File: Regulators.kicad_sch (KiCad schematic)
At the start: 34 parts, among them J3 Conn_01x02_Socket, U10 TPS5430DDAR, U2 TPS5430DDAR, U9 TPS5430DDAR

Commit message: Initial tidy of untracked files
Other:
- note added: "Todo - redo regulators once you know the current draw of all device, ideally within the 60-70% range of current limit for peak efficiency"
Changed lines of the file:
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@@
+		)
+	)
+	(text "Todo - redo regulators once you know the current draw of all device, \nideally within the 60-70% range of current limit for peak efficiency"
+		(exclude_from_sim no)
+		(at 161.036 19.304 0)
+		(effects
+			(font
+				(size 1.27 1.27)
+			)
 		)
 	)

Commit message: Changed board spec from Nucleo F446RE to F446ZE Altered readme to suit it and moved the Todos over.
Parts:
- C16, C17, C18, C2, C20, C21: footprint (none) -> Capacitor_SMD:C_1206_3216Metric_Pad1.33x1.80mm_HandSolder
- D1, D2, D3, D6, D7, D8: footprint (none) -> Diode_SMD:D_1206_3216Metric_Pad1.42x1.75mm_HandSolder
- R10, R11, R2, R3, R4, R5, R6, R8, R9: footprint (none) -> Resistor_SMD:R_1206_3216Metric_Pad1.30x1.75mm_HandSolder
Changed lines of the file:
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@@
 			)
 		)
-		(property "Footprint" ""
+		(property "Footprint" "Resistor_SMD:R_1206_3216Metric_Pad1.30x1.75mm_HandSolder"
 			(at 131.826 117.094 90)
 			(effects
@@
 			)
 		)
-		(property "Footprint" ""
+		(property "Footprint" "Resistor_SMD:R_1206_3216Metric_Pad1.30x1.75mm_HandSolder"
 			(at 199.136 77.724 90)
 			(effects
@@
 			)
 		)
-		(property "Footprint" ""
+		(property "Footprint" "Capacitor_SMD:C_1206_3216Metric_Pad1.33x1.80mm_HandSolder"
 			(at 85.09 108.2548 0)
 			(effects
@@
 			)
 		)
-		(property "Footprint" ""
+		(property "Footprint" "Capacitor_SMD:C_1206_3216Metric_Pad1.33x1.80mm_HandSolder"
 			(at 101.2952 53.34 0)
 			(effects
@@
 			)
 		)
-		(property "Footprint" ""
+		(property "Footprint" "Capacitor_SMD:C_1206_3216Metric_Pad1.33x1.80mm_HandSolder"
 			(at 152.4 42.2148 0)
 			(effects
@@
 			)
 		)
-		(property "Footprint" ""
+		(property "Footprint" "Resistor_SMD:R_1206_3216Metric_Pad1.30x1.75mm_HandSolder"
 			(at 265.176 117.094 90)
 			(effects
@@
 			)
 		)
-		(property "Footprint" ""
+		(property "Footprint" "Capacitor_SMD:C_1206_3216Metric_Pad1.33x1.80mm_HandSolder"
 			(at 33.9852 119.38 0)
 			(effects
@@
 			)
 		)
-		(property "Footprint" ""
+		(property "Footprint" "Resistor_SMD:R_1206_3216Metric_Pad1.30x1.75mm_HandSolder"
 			(at 265.176 143.764 90)
 			(effects
@@
 			)
 		)
-		(property "Footprint" ""
+		(property "Footprint" "Resistor_SMD:R_1206_3216Metric_Pad1.30x1.75mm_HandSolder"
 			(at 253.746 42.164 90)
 			(effects
@@
 			)
 		)
-		(property "Footprint" ""
+		(property "Footprint" "Diode_SMD:D_1206_3216Metric_Pad1.42x1.75mm_HandSolder"
 			(at 252.73 52.07 0)
 			(effects
@@
 			)
 		)
-		(property "Footprint" ""
+		(property "Footprint" "Diode_SMD:D_1206_3216Metric_Pad1.42x1.75mm_HandSolder"
 			(at 237.49 52.07 0)
 			(effects
@@
 			)
 		)
-		(property "Footprint" ""
+		(property "Footprint" "Diode_SMD:D_1206_3216Metric_Pad1.42x1.75mm_HandSolder"
 			(at 267.97 52.07 0)
 			(effects
@@
 			)
 		)
-		(property "Footprint" ""
+		(property "Footprint" "Capacitor_SMD:C_1206_3216Metric_Pad1.33x1.80mm_HandSolder"
 			(at 218.44 108.2548 0)
 			(effects
@@
 			)
 		)
-		(property "Footprint" ""
+		(property "Footprint" "Diode_SMD:D_1206_3216Metric_Pad1.42x1.75mm_HandSolder"
 			(at 165.1 52.07 0)
 			(effects
@@
 			)
 		)
-		(property "Footprint" ""
+		(property "Footprint" "Capacitor_SMD:C_1206_3216Metric_Pad1.33x1.80mm_HandSolder"
 			(at 167.3352 119.38 0)
 			(effects
@@
 			)
 		)
-		(property "Footprint" ""
+		(property "Footprint" "Resistor_SMD:R_1206_3216Metric_Pad1.30x1.75mm_HandSolder"
 			(at 131.826 143.764 90)
 			(effects
@@
 			)
 		)
-		(property "Footprint" ""
+		(property "Footprint" "Resistor_SMD:R_1206_3216Metric_Pad1.30x1.75mm_HandSolder"
 			(at 199.136 51.054 90)
 			(effects
@@
 			)
 		)
-		(property "Footprint" ""
+		(property "Footprint" "Diode_SMD:D_1206_3216Metric_Pad1.42x1.75mm_HandSolder"
 			(at 97.79 118.11 0)
 			(effects
@@
 			)
 		)
-		(property "Footprint" ""
+		(property "Footprint" "Resistor_SMD:R_1206_3216Metric_Pad1.30x1.75mm_HandSolder"
 			(at 238.506 42.164 90)
 			(effects
@@
 			)
 		)
-		(property "Footprint" ""
+		(property "Footprint" "Diode_SMD:D_1206_3216Metric_Pad1.42x1.75mm_HandSolder"
 			(at 231.14 118.11 0)
 			(effects
@@
 			)
 		)
-		(property "Footprint" ""
+		(property "Footprint" "Resistor_SMD:R_1206_3216Metric_Pad1.30x1.75mm_HandSolder"
 			(at 268.986 42.164 90)
 			(effects

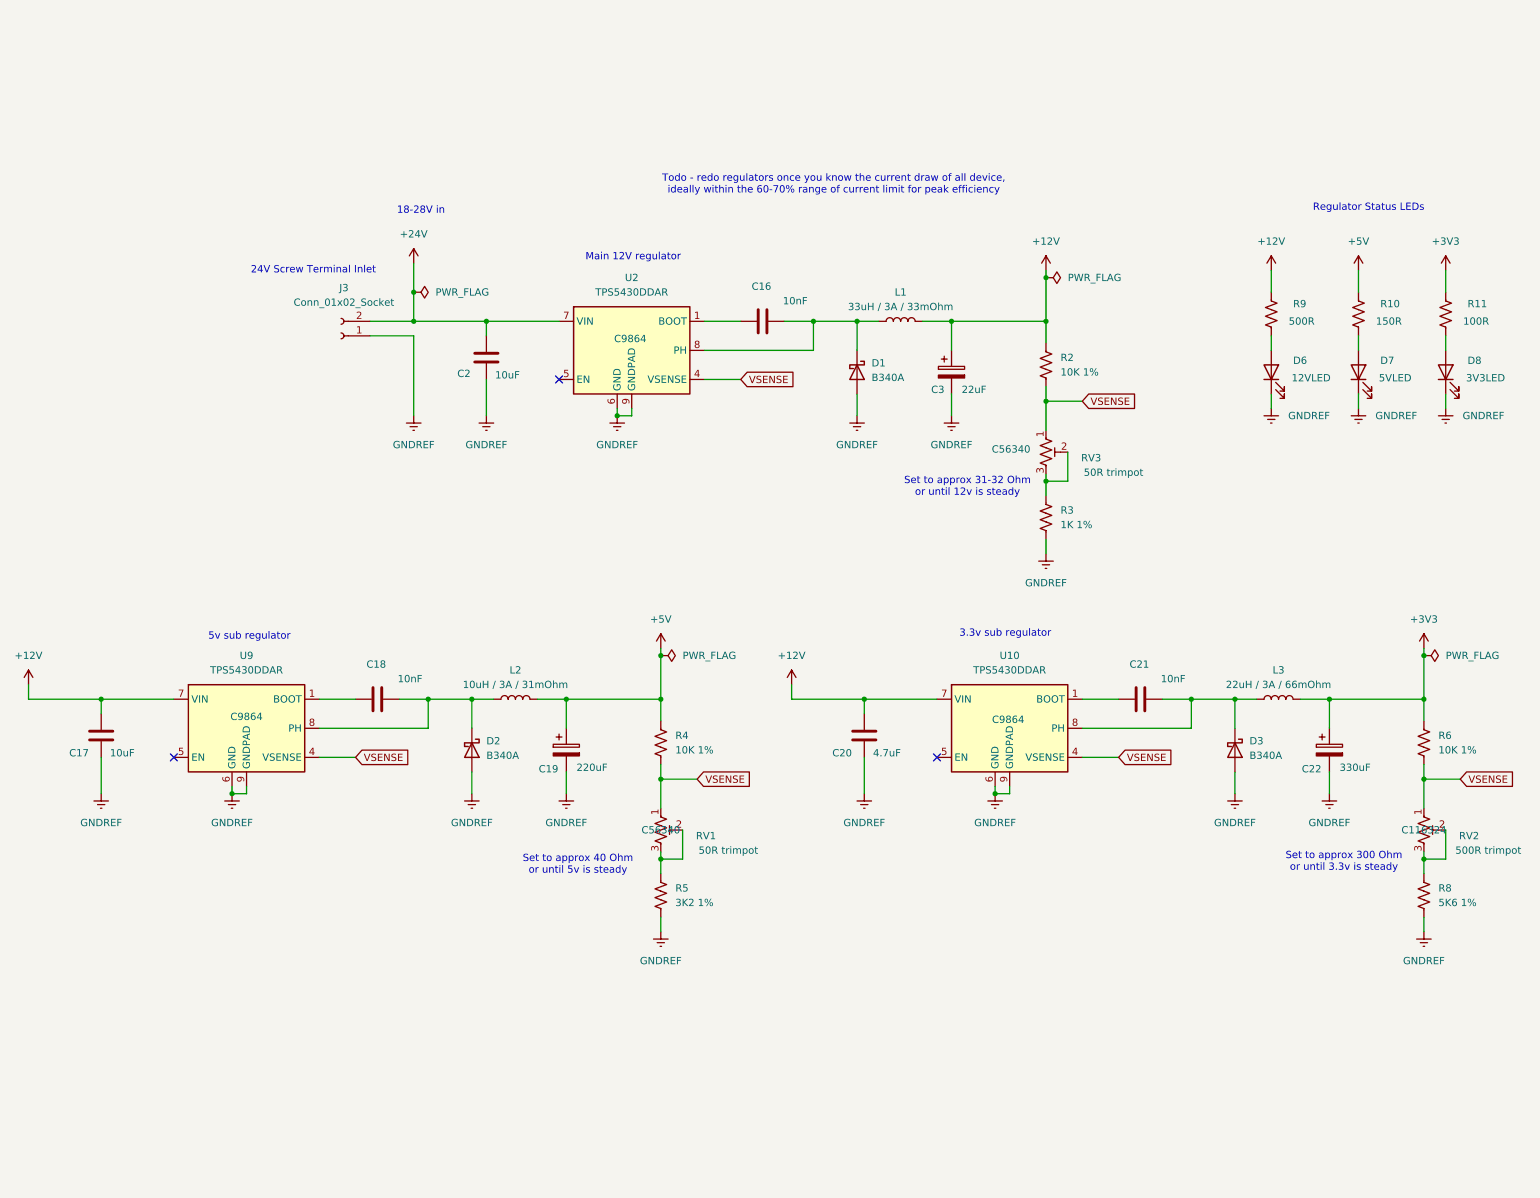
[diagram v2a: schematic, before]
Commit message: changes some unecessary global labels to local. Added a heirarchical sheet for output driver and basic numbering. Sink logic not yet set for O/Ps, but placeholder for now
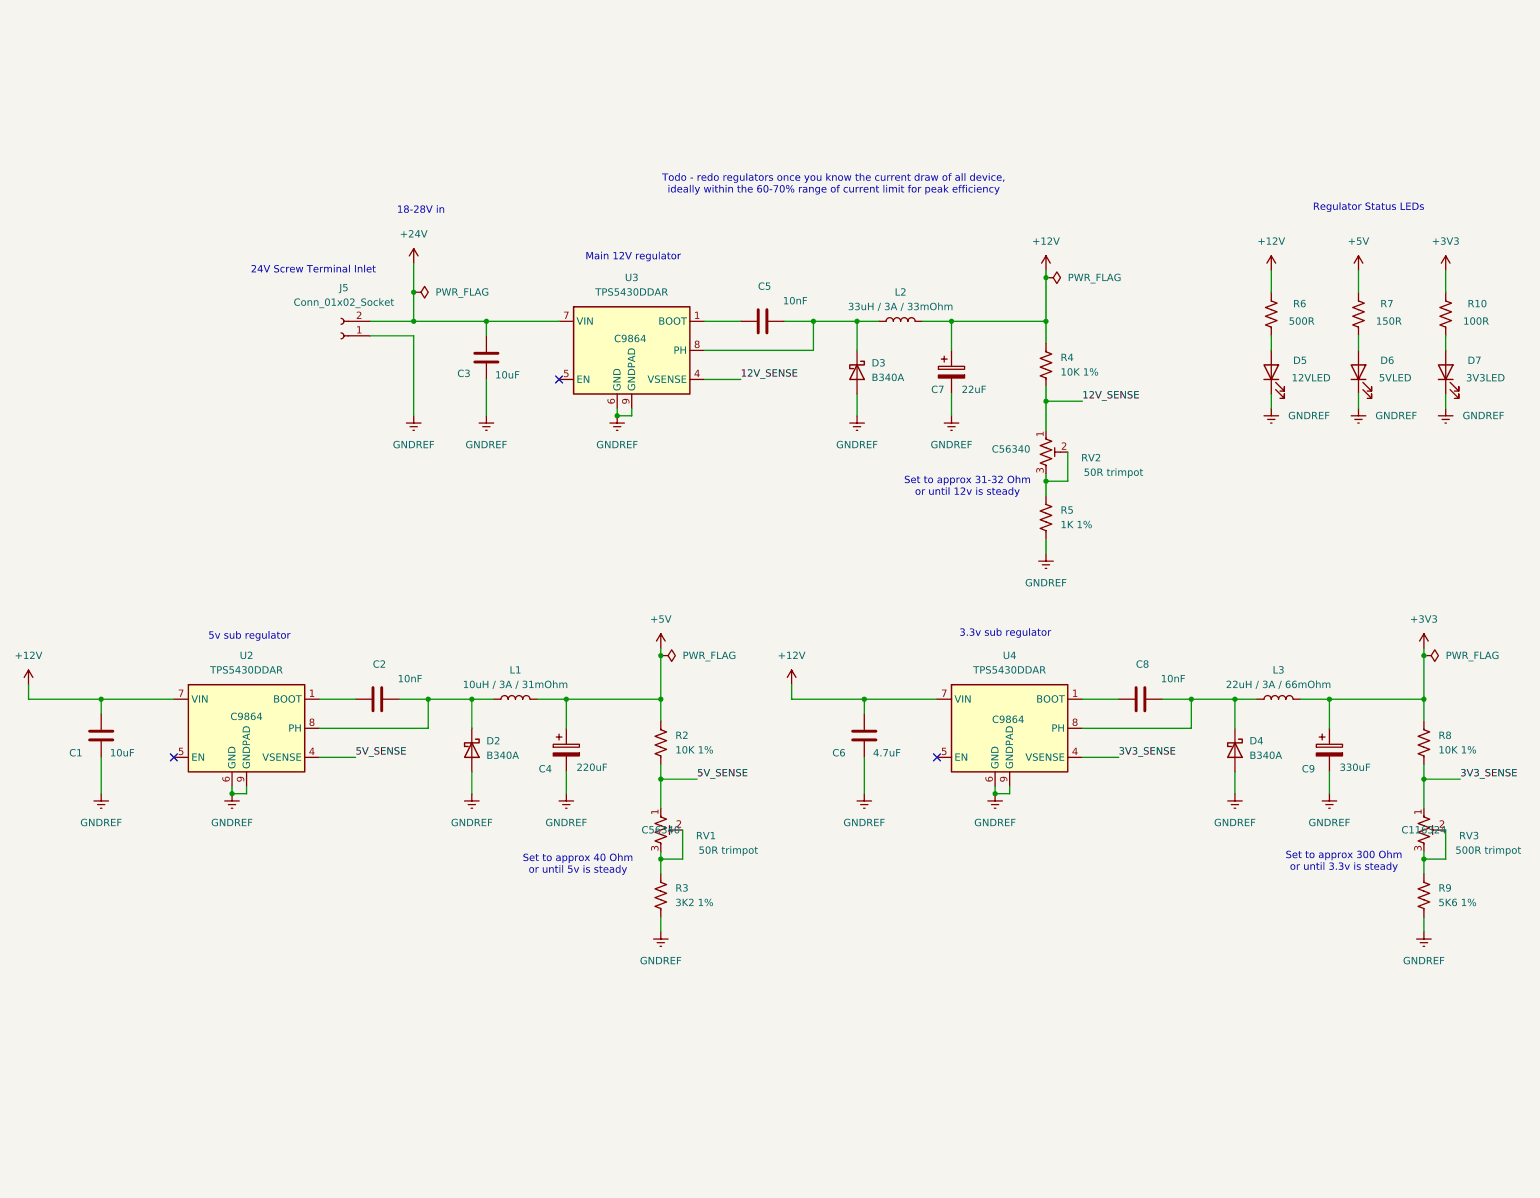
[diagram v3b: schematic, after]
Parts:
- renumbered C17 to C1, C18 to C2, C2 to C3, C19 to C4, C16 to C5, C20 to C6, C3 to C7, C21 to C8, C22 to C9, D1 to D3, D3 to D4, D6 to D5, D7 to D6, D8 to D7, J3 to J5, L2 to L1, L1 to L2, R11 to R10, R4 to R2, R5 to R3, R2 to R4, R3 to R5, R9 to R6, R10 to R7, R6 to R8, R8 to R9, RV3 to RV2, RV2 to RV3, U9 to U2, U2 to U3, U10 to U4
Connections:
- removed net VSENSE: R2.2, R4.2, R8.2, RV1.1, RV2.1, RV3.1, U2.4 (VSENSE), U3.4 (VSENSE), U4.4 (VSENSE)
- new net 12V_SENSE: R4.2, RV2.1, U3.4 (VSENSE)
- new net 3V3_SENSE: R8.2, RV3.1, U4.4 (VSENSE)
- new net 5V_SENSE: R2.2, RV1.1, U2.4 (VSENSE)

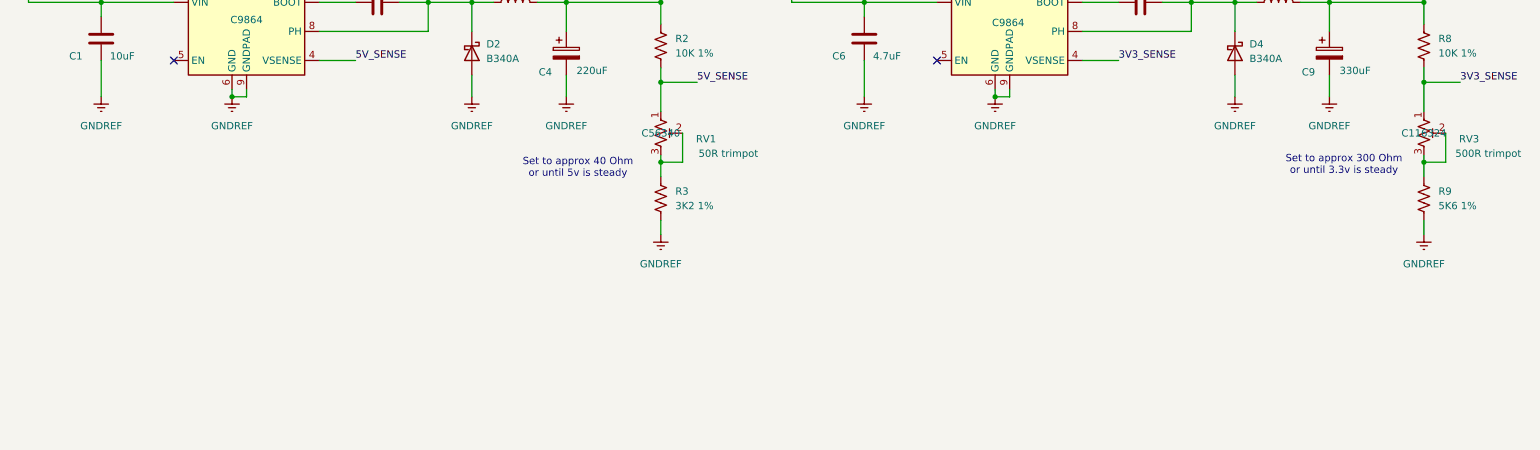
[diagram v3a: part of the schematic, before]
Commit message: redrew stepper drivers as duplicatable heirarchical sheets, moved jumpers into power managemente sheet, moved LEDs and user buttons into own sheet to save space. Fixed a few random labelling issues.
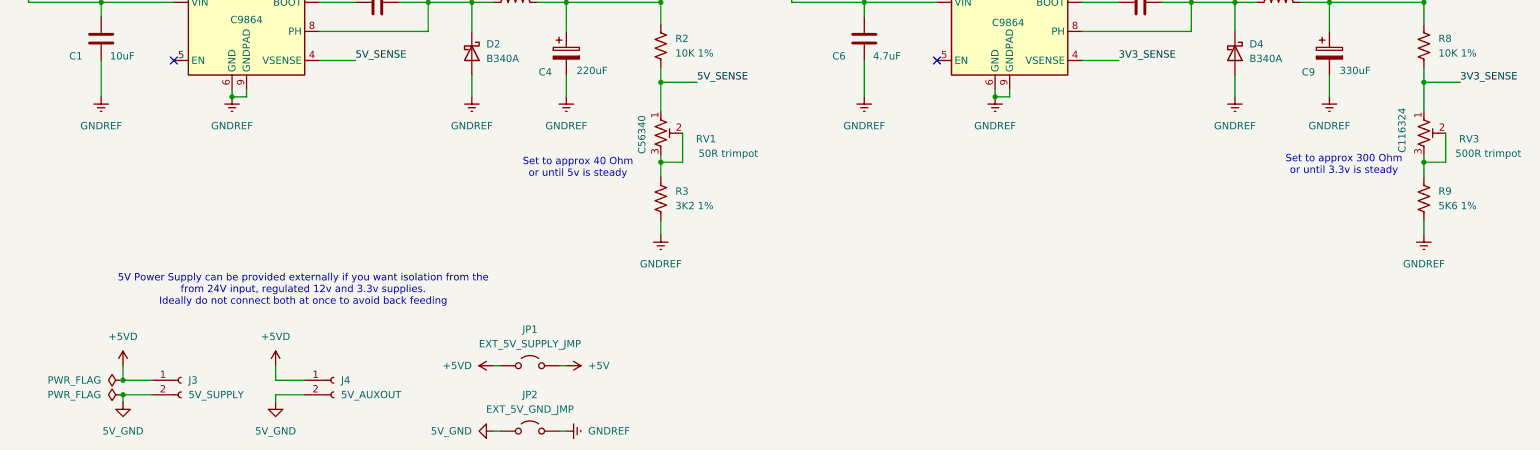
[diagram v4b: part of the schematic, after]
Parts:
- added J3: 5V_SUPPLY, symbol Connector:Conn_01x02_Socket
- added J4: 5V_AUXOUT, symbol Connector:Conn_01x02_Socket
- added JP1: EXT_5V_SUPPLY_JMP, Jumper:SolderJumper-2_P1.3mm_Open_TrianglePad1.0x1.5mm, symbol Jumper:Jumper_2_Open
- added JP2: EXT_5V_GND_JMP, Jumper:SolderJumper-2_P1.3mm_Open_TrianglePad1.0x1.5mm, symbol Jumper:Jumper_2_Open
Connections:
- net +5V: now also JP1.2 (B)
- net GNDREF: now also JP2.2 (B)
- new net +5VD: J3.1 (Pin_1), J4.1 (Pin_1), JP1.1 (A)
- new net 5V_GND: J3.2 (Pin_2), J4.2 (Pin_2), JP2.1 (A)
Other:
- note added: "5V Power Supply can be provided externally if you want isolation from the from 24V input, regulated 12v and 3.3v supplies. Ideally do not connect both at once to avoid back feeding"

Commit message: Completed design for digital outputs, tidied into own sheets and bussing for scalability
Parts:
- renumbered C9 to C10, C1 to C2, C2 to C3, C3 to C4, C4 to C5, C5 to C6, C6 to C7, C7 to C8, C8 to C9, J3 to J4, J4 to J5, J5 to J6

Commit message: tidy of some sheets. Added 0-10V DAC, but untested - only some basic validation on simulator for now
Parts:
- C10, C5, C8: footprint (none) -> Capacitor_SMD:C_1206_3216Metric_Pad1.33x1.80mm_HandSolder
- C4, C7, C9: footprint Capacitor_SMD:C_1206_3216Metric_Pad1.33x1.80mm_HandSolder -> (none)
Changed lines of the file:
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@@
 			)
 		)
-		(property "Footprint" "Capacitor_SMD:C_1206_3216Metric_Pad1.33x1.80mm_HandSolder"
+		(property "Footprint" ""
 			(at 101.2952 53.34 0)
 			(effects
@@
 			)
 		)
-		(property "Footprint" ""
+		(property "Footprint" "Capacitor_SMD:C_1206_3216Metric_Pad1.33x1.80mm_HandSolder"
 			(at 115.2652 121.92 0)
 			(effects
@@
 			)
 		)
-		(property "Footprint" ""
+		(property "Footprint" "Capacitor_SMD:C_1206_3216Metric_Pad1.33x1.80mm_HandSolder"
 			(at 248.6152 121.92 0)
 			(effects
@@
 			)
 		)
-		(property "Footprint" ""
+		(property "Footprint" "Capacitor_SMD:C_1206_3216Metric_Pad1.33x1.80mm_HandSolder"
 			(at 182.5752 55.88 0)
 			(effects
@@
 			)
 		)
-		(property "Footprint" "Capacitor_SMD:C_1206_3216Metric_Pad1.33x1.80mm_HandSolder"
+		(property "Footprint" ""
 			(at 218.44 108.2548 0)
 			(effects
@@
 			)
 		)
-		(property "Footprint" "Capacitor_SMD:C_1206_3216Metric_Pad1.33x1.80mm_HandSolder"
+		(property "Footprint" ""
 			(at 167.3352 119.38 0)
 			(effects

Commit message: Deleted stale test production files. Fixed up a bug with power isolation. Created some footprints for wire to board connectors although ran out of time to fix a bug where they do no lock in. Fixes to readme
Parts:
- C1: renamed from C2; footprint Capacitor_SMD:C_1206_3216Metric_Pad1.33x1.80mm_HandSolder -> (none)
- C4: renamed from C5; footprint Capacitor_SMD:C_1206_3216Metric_Pad1.33x1.80mm_HandSolder -> (none)
- C7: renamed from C8; footprint Capacitor_SMD:C_1206_3216Metric_Pad1.33x1.80mm_HandSolder -> (none)
- C8: renamed from C9; footprint (none) -> Capacitor_SMD:C_1206_3216Metric_Pad1.33x1.80mm_HandSolder
- C9: renamed from C10; footprint Capacitor_SMD:C_1206_3216Metric_Pad1.33x1.80mm_HandSolder -> (none)
- J3: renamed from J4; footprint (none) -> OSTVTerminalBlocks:Conn01x02
- J4: renamed from J5; footprint (none) -> OSTVTerminalBlocks:Conn01x02
- J5: renamed from J6; value Conn_01x02_Socket -> 24V Power Inlet; footprint (none) -> OSTVTerminalBlocks:Conn01x02
- renumbered C3 to C2, C4 to C3, C6 to C5, C7 to C6
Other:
- note removed: "24V Screw Terminal Inlet"
